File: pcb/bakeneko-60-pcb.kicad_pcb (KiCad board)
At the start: 2 copper layers, 284.7 x 94.2 mm, 154 parts, among them J1 JST SH 4-pin, J2 AVR-ISP-6, SW1 Reset, U1 SRV05-4, U2 ATmega32U4-AU, Y1 16MHz

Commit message: Fiddle with settings for Gerbers
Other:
- rule pad_to_mask_clearance: 0.05 -> 0
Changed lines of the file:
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@@
   )
   (setup
-    (pad_to_mask_clearance 0.05)
+    (stackup
+      (layer "F.SilkS" (type "Top Silk Screen"))
+      (layer "F.Paste" (type "Top Solder Paste"))
+      (layer "F.Mask" (type "Top Solder Mask") (thickness 0.01))
+      (layer "F.Cu" (type "copper") (thickness 0.035))
+      (layer "dielectric 1" (type "core") (thickness 1.51) (material "FR4") (epsilon_r 4.5) (loss_tangent 0.02))
+      (layer "B.Cu" (type "copper") (thickness 0.035))
+      (layer "B.Mask" (type "Bottom Solder Mask") (thickness 0.01))
+      (layer "B.Paste" (type "Bottom Solder Paste"))
+      (layer "B.SilkS" (type "Bottom Silk Screen"))
+      (copper_finish "None")
+      (dielectric_constraints no)
+    )
+    (pad_to_mask_clearance 0)
+    (aux_axis_origin -0.53625 94.74)
     (grid_origin 4.60375 43.18)
     (pcbplotparams
@@
     (pad "4" smd roundrect locked (at 1.5 2 270) (size 0.6 1.55) (layers "B.Cu" "B.Paste" "B.Mask") (roundrect_rratio 0.25)
       (net 1 "GND"))
-    (pad "MP" smd roundrect locked (at -2.8 -1.875 270) (size 1.2 1.8) (layers "B.Cu" "B.Paste" "B.Mask") (roundrect_rratio 0.208333))
-    (pad "MP" smd roundrect locked (at 2.8 -1.875 270) (size 1.2 1.8) (layers "B.Cu" "B.Paste" "B.Mask") (roundrect_rratio 0.208333))
+    (pad "MP" smd roundrect locked (at -2.8 -1.875 270) (size 1.2 1.8) (layers "B.Cu" "B.Paste" "B.Mask") (roundrect_rratio 0.2083333333))
+    (pad "MP" smd roundrect locked (at 2.8 -1.875 270) (size 1.2 1.8) (layers "B.Cu" "B.Paste" "B.Mask") (roundrect_rratio 0.2083333333))
     (model "${KISYS3DMOD}/Connector_JST.3dshapes/JST_SH_SM04B-SRSS-TB_1x04-1MP_P1.00mm_Horizontal.wrl"
       (offset (xyz 0 0 0))

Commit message: Add some funny text
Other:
- board text added: "This Is Not A PCB"
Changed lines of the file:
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@@
   (gr_line (start 284.7 91.95) (end 284.7 2.25) (layer "Edge.Cuts") (width 0.2))
   (gr_arc (start 249.918072 0.806452) (mid 250.470392 0.217362) (end 251.248106 0) (layer "Edge.Cuts") (width 0.2))
-  (gr_text "Unbakeneko60 v0.1" (at 274.915477 91.907501) (layer "B.SilkS")
+  (gr_text "This Is Not A PCB" (at 9.39375 91.73) (layer "B.SilkS")
     (effects (font (size 1 1) (thickness 0.15)) (justify mirror))
   )
+  (gr_text "Unbakeneko60 v0.1" (at 274.82375 91.77) (layer "B.SilkS")
+    (effects (font (size 1 1) (thickness 0.15)) (justify mirror))
+  )

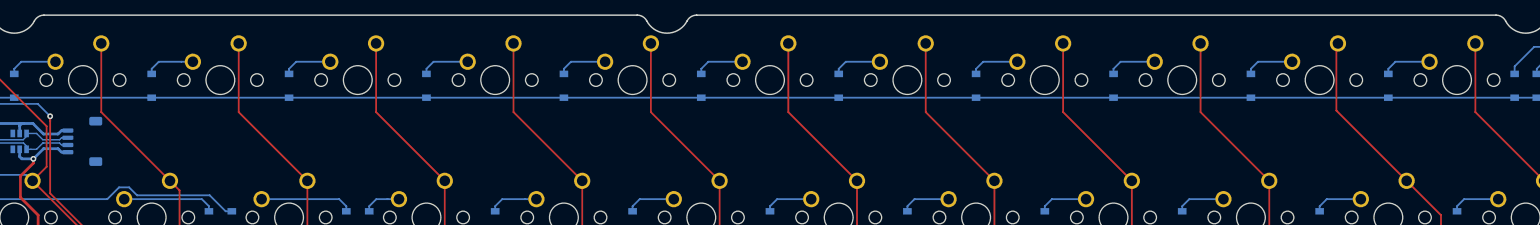
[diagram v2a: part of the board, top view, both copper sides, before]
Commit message: Convert three 1u in top row to hotswap
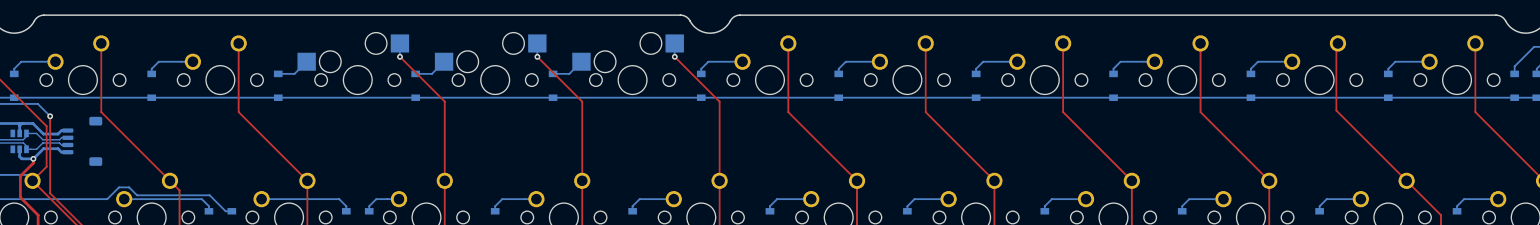
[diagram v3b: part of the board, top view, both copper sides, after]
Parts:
- MX5, MX6, MX7: footprint MX_Only:MXOnly-1U-NoLED -> MX_Only:MXOnly-1U-Hotswap
- moved D5 1.50 mm to (74.2, 9.79)
- moved D6 1.50 mm to (93.2, 9.79)
- moved D7 1.50 mm to (112.3, 9.79)
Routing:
- net Net-(D5-Pad2): track 6.82 -> 4.64 mm
- net Net-(D7-Pad2): track 6.82 -> 4.64 mm
- net Net-(D6-Pad2): track 6.82 -> 4.64 mm
- net COL4: track 168.2 -> 166.9 mm, vias 0 -> 1
- net COL5: track 161.8 -> 160.4 mm, vias 0 -> 1
- net COL6: track 209.7 -> 208.3 mm, vias 0 -> 1
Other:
- outline, holes or cut-outs redrawn

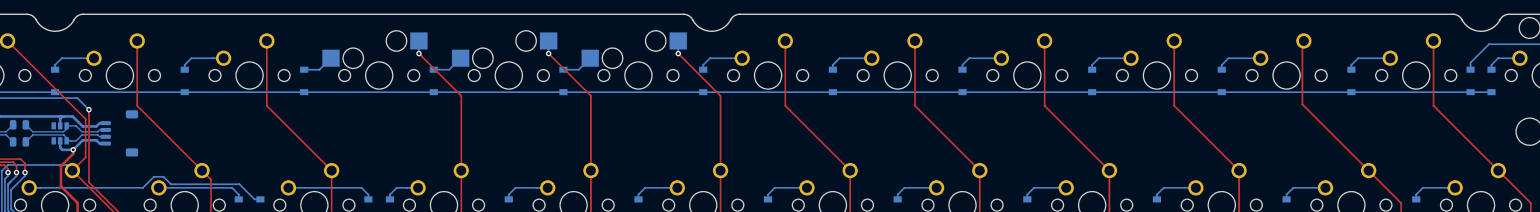
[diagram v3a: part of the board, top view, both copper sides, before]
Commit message: Convert more 1u top row to hotswap
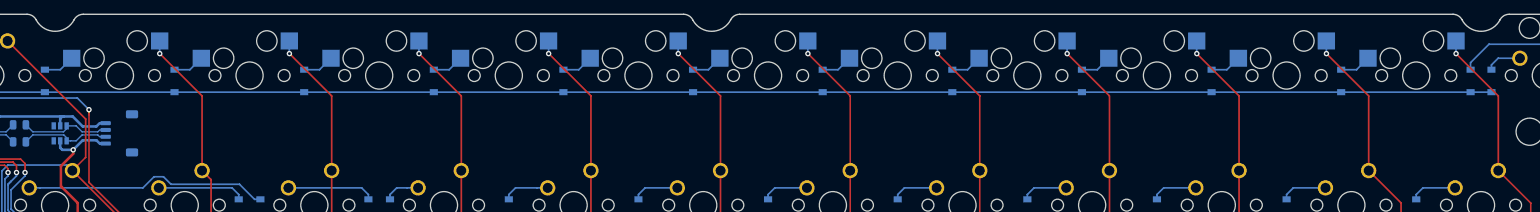
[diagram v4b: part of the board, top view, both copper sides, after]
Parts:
- MX10, MX11, MX12, MX13, MX3, MX4, MX8, MX9: footprint MX_Only:MXOnly-1U-NoLED -> MX_Only:MXOnly-1U-Hotswap
- moved D10 1.50 mm to (169.4, 9.79)
- moved D11 1.50 mm to (188.5, 9.79)
- moved D12 1.50 mm to (207.5, 9.79)
- moved D13 1.50 mm to (226.6, 9.79)
- moved D3 1.50 mm to (36.1, 9.79)
- moved D4 1.50 mm to (55.1, 9.79)
- moved D8 1.50 mm to (131.3, 9.79)
- moved D9 1.50 mm to (150.4, 9.79)
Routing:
- net Net-(D9-Pad2): track 6.82 -> 4.64 mm
- net Net-(D12-Pad2): track 6.82 -> 4.64 mm
- net Net-(D4-Pad2): track 6.82 -> 4.64 mm
- net Net-(D11-Pad2): track 6.82 -> 4.64 mm
- net Net-(D3-Pad2): track 6.82 -> 4.64 mm
- net Net-(D8-Pad2): track 6.82 -> 4.64 mm
- net Net-(D13-Pad2): track 6.82 -> 4.64 mm
- net Net-(D10-Pad2): track 6.82 -> 4.64 mm
- net COL11: track 292.8 -> 291.2 mm, vias 0 -> 1
- net COL12: track 323.1 -> 321.7 mm, vias 0 -> 1
- net COL10: track 274.7 -> 273.3 mm, vias 0 -> 1
- net COL3: track 125.1 -> 123.7 mm, vias 0 -> 1
- net COL2: track 144.2 -> 142.8 mm, vias 2 -> 3
- net COL9: track 236.0 -> 234.7 mm, vias 0 -> 1
- net COL8: track 242.2 -> 240.8 mm, vias 0 -> 1
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
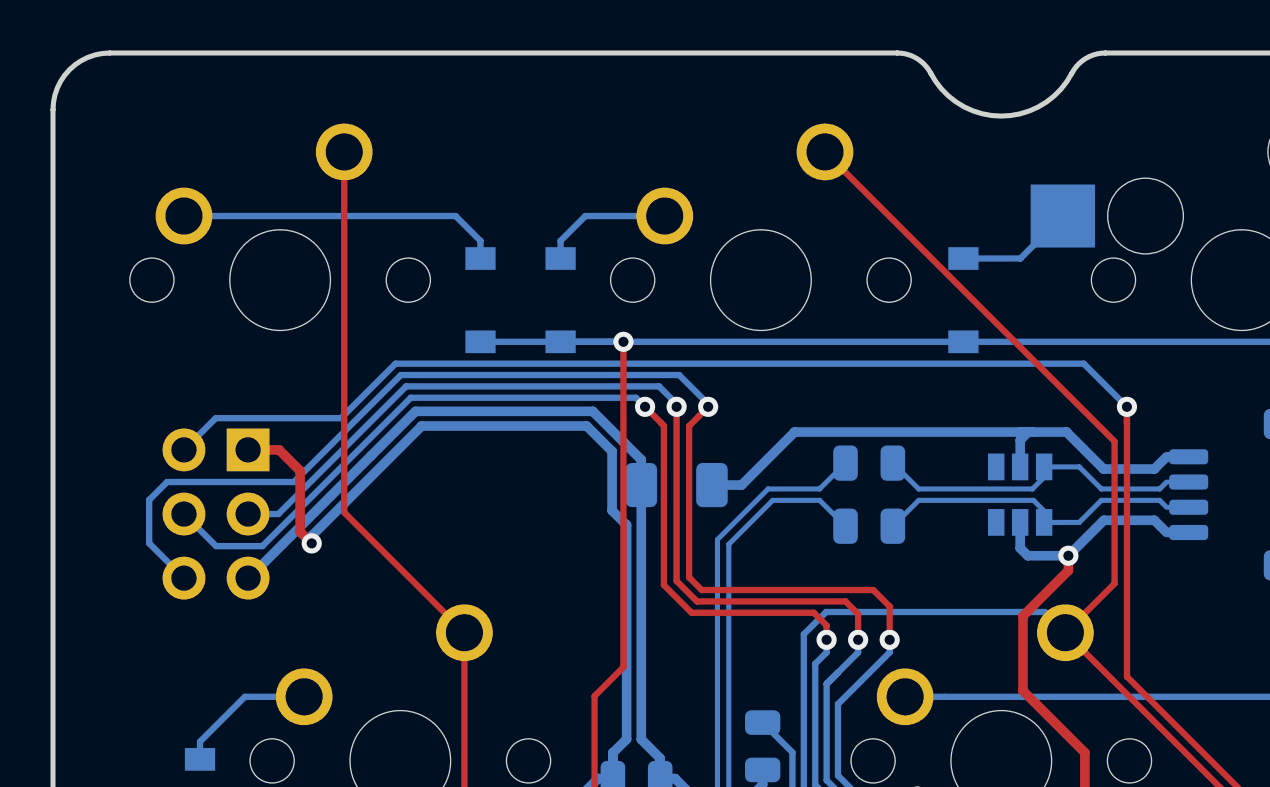
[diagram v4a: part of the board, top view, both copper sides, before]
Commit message: Convert first two top row keys to hotswap
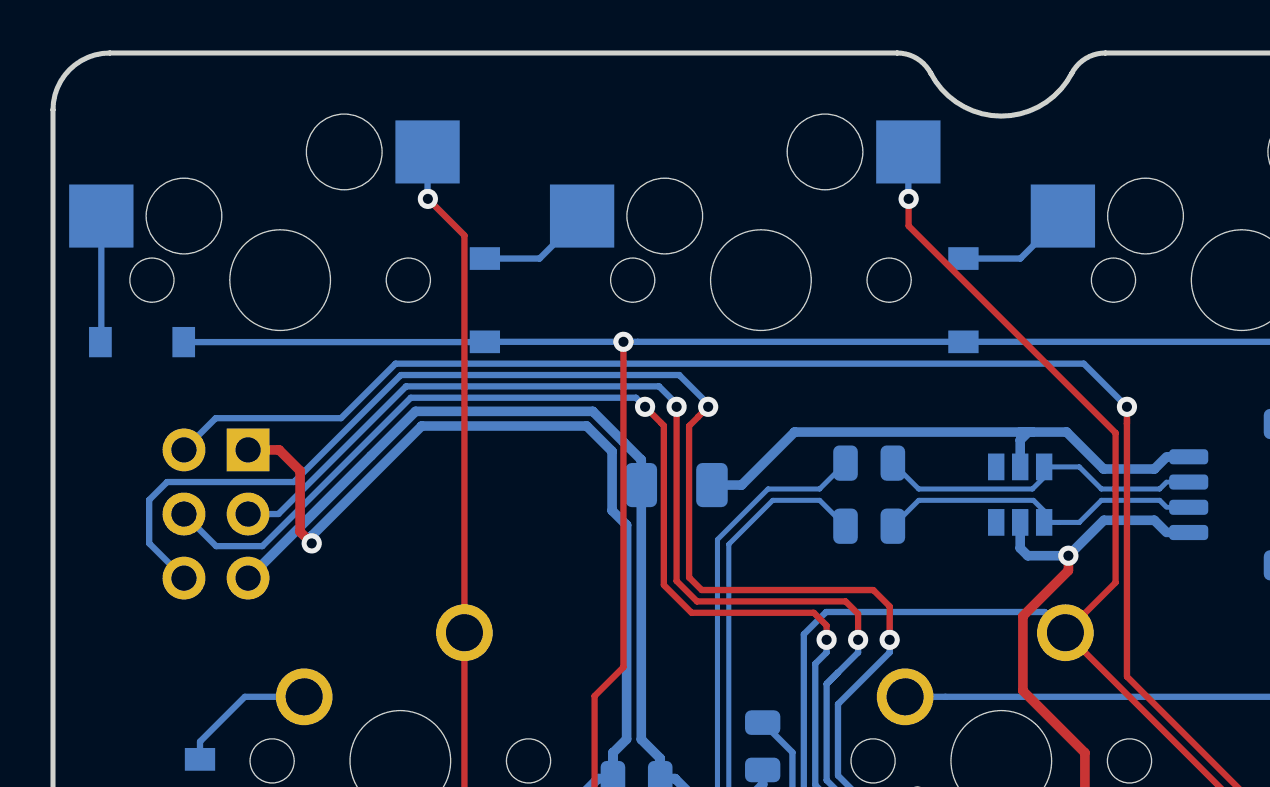
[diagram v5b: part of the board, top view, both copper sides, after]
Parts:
- MX1, MX2: footprint MX_Only:MXOnly-1U-NoLED -> MX_Only:MXOnly-1U-Hotswap
- moved D1 13.5 mm to (3.53, 11.5), turned to 180 degrees
- moved D2 3.00 mm to (17.1, 9.79)
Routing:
- net ROW0: track 257.1 -> 266.5 mm
- net Net-(D1-Pad2): track 12.9 -> 5.01 mm
- net COL0: track 100.2 -> 98.9 mm, vias 1 -> 2
- net COL1: track 110.2 -> 108.9 mm, vias 0 -> 1
- net Net-(D2-Pad2): track 5.23 -> 4.55 mm

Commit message: Convert remaining top row to hotswap
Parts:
- removed the D14 at (248.7, 9.79)
- removed the MX14 at (256.6, 9.00)
- removed MX15: 1u, MX_Only:MXOnly-1U-NoLED
- MX14: renamed from MX16; footprint MX_Only:MXOnly-2U-NoLED -> MX_Only:MXOnly-2U-Hotswap
- moved D14 9.60 mm to (255.2, 9.79)
- renumbered D15 to D14
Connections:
- MX14 pad 2: COL14 -> COL13
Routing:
- net COL14: track 314.2 -> 0.00 mm, vias 1 -> 0
- net Net-(D14-Pad2): track 29.3 -> 4.60 mm
- net ROW0: track 266.5 -> 273.1 mm
- net COL13: track 349.5 -> 344.1 mm, vias 0 -> 1
- net Net-(D14-Pad2) (its old number): track 5.29 -> 0.00 mm
- net ROW2: track 270.3 -> 267.5 mm
